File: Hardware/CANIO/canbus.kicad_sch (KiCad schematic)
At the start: 3 parts, among them J201 CAN, J202 CAN, U201 MCP25625-x-SS

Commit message: Add more boilerplate
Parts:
- added C201, C202: 22pf, Capacitor_SMD:C_0201_0603Metric, symbol Device:C_Small
- added C203, C204, C205: 100nf, Capacitor_SMD:C_0805_2012Metric, symbol Device:C_Small
- added R201: 120R, Resistor_THT:R_Axial_DIN0207_L6.3mm_D2.5mm_P10.16mm_Horizontal, symbol Device:R_Small
- added R202: 120R, Resistor_SMD:R_0805_2012Metric, symbol Device:R_Small
- added Y201: 16mHz, Crystal:Crystal_SMD_HC49-SD, symbol Device:Crystal
- J201, J202: footprint (none) -> Connector_Wire:SolderWire-0.5sqmm_1x02_P4.8mm_D0.9mm_OD2.3mm_Relief
- U201: LCSC# (none) -> C628816
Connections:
- net +5V: now also U201.1 (VIO), U201.19 (VDD), C203.1, C204.1, C205.1
- net CANH: now also R201.2
- net CANL: now also R201.1
- net GND: now reaches U201.10 (GND)
- net GND: now also U201.26 (VSS), C201.1, C202.2, C203.2, C204.2, C205.2, R202.1
- net SCK: now reaches U201.14 (SCK)
- net SI: now reaches U201.15 (SI)
- net SO: now reaches U201.16 (SO)
- net CS: now reaches U201.17 (~{CS})
- net CLKOUT: now reaches U201.22 (CLKOUT)
- net at U201.5 (STBY): now also R202.2
- net at U201.8 (OSC2): now also C202.1, Y201.1
- net at U201.9 (OSC1): now also C201.2, Y201.2
- no-connect marks 0 -> 7

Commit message: Add processor
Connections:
- net INT: now reaches U201.13 (~{INT})
- net STBY: now reaches R202.2, U201.5 (STBY)
- no-connect marks 7 -> 6
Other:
- note added: "INT lets us know if there is activity we need to see"
- note added: "Im not really planning on using standby mode, but the chip does offer some nice power saving and resume options! See page 7 in the datasheet for details"
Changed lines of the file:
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@@
   (junction (at 184.785 109.855) (diameter 0) (color 0 0 0 0)
+  )
+  (junction (at 108.585 78.105) (diameter 0) (color 0 0 0 0)
   )
   (junction (at 141.605 71.755) (diameter 0) (color 0 0 0 0)
@@
   (no_connect (at 131.445 113.665))
   (no_connect (at 131.445 100.965))
-  (no_connect (at 131.445 118.745))
   (no_connect (at 131.445 103.505))
+  (wire (pts (xy 125.73 118.745) (xy 131.445 118.745))
+    (stroke (width 0) (type default))
+  )
   (wire (pts (xy 141.605 71.755) (xy 141.605 73.025))
     (stroke (width 0) (type default))
@@
     (stroke (width 0) (type default))
   )
+  (wire (pts (xy 99.695 78.105) (xy 108.585 78.105))
+    (stroke (width 0) (type default))
+  )
   (wire (pts (xy 243.84 69.85) (xy 234.95 69.85))
     (stroke (width 0) (type default))
@@
     (stroke (width 0) (type default))
   )
+  (text "INT lets us know\nif there is activity\nwe need to see"
+    (at 100.965 120.65 0)
+    (effects (font (size 1.27 1.27)) (justify left bottom))
+  )
+  (text "Im not really planning\non using standby mode, but the\nchip does offer some nice\npower saving and resume options!\n\nSee page 7 in the datasheet for details"
+    (at 52.07 87.63 0)
+    (effects (font (size 1.27 1.27)) (justify left bottom))
+  )
   (label "CANL" (at 170.815 80.645 180) (fields_autoplaced)
     (effects (font (size 1.27 1.27)) (justify right bottom))
@@
     (effects (font (size 1.27 1.27)) (justify right))
   )
+  (hierarchical_label "INT" (shape output) (at 125.73 118.745 180) (fields_autoplaced)
+    (effects (font (size 1.27 1.27)) (justify right))
+  )
   (hierarchical_label "SO" (shape output) (at 125.73 88.265 180) (fields_autoplaced)
     (effects (font (size 1.27 1.27)) (justify right))
@@
     (effects (font (size 1.27 1.27)) (justify right))
   )
+  (hierarchical_label "STBY" (shape input) (at 99.695 78.105 180) (fields_autoplaced)
+    (effects (font (size 1.27 1.27)) (justify right))
+  )

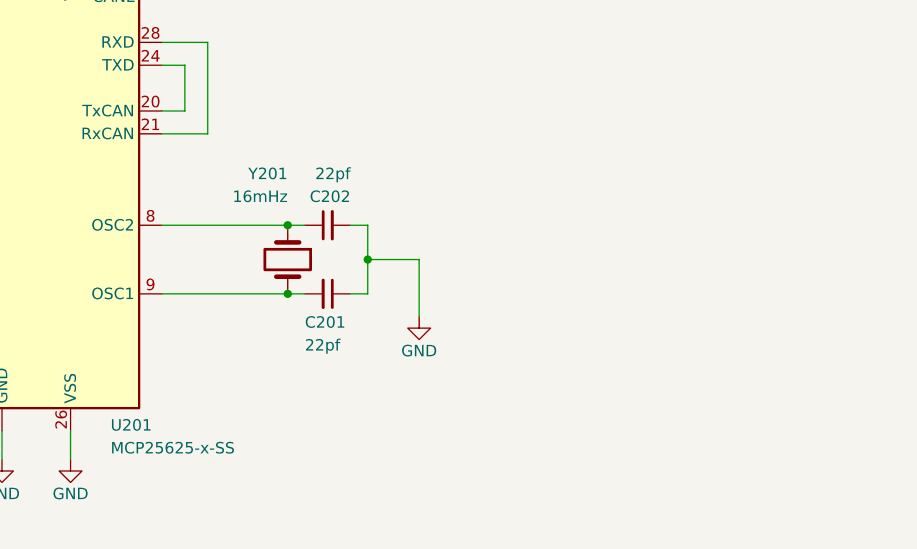
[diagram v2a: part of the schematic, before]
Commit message: Edge cuts and stuff
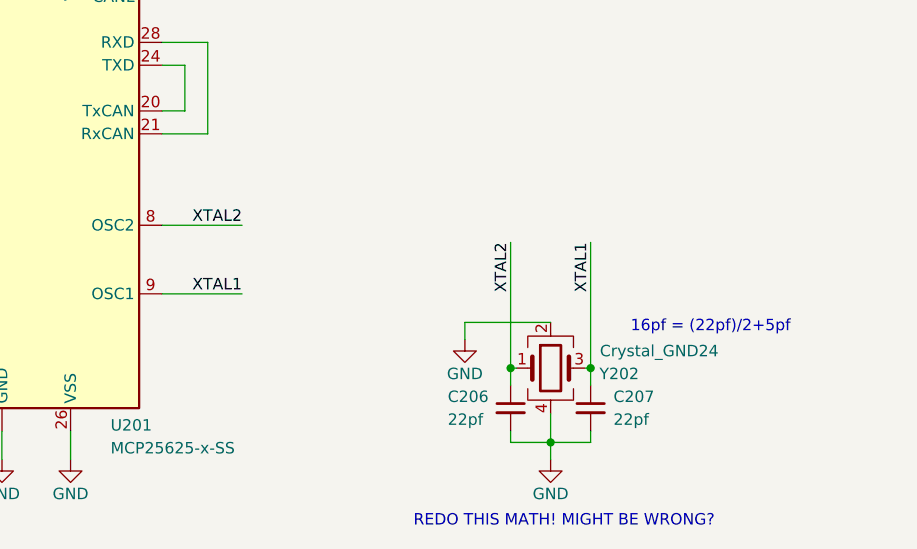
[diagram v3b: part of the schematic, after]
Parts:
- removed C201, C202: 22pf, Capacitor_SMD:C_0201_0603Metric, symbol Device:C_Small
- removed Y201: 16mHz, Crystal:Crystal_SMD_HC49-SD, symbol Device:Crystal
- added C206, C207: 22pf, Capacitor_SMD:C_0603_1608Metric, symbol Device:C_Small
- added Y202: Crystal_GND24, Crystal:Crystal_SMD_3225-4Pin_3.2x2.5mm, symbol Device:Crystal_GND24
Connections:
- net GND: now also C206.2, C207.2, Y202.2, Y202.4
- net XTAL2: now reaches U201.8 (OSC2)
- net XTAL2: now also C206.1, Y202.1
- net XTAL1: now reaches U201.9 (OSC1)
- net XTAL1: now also C207.1, Y202.3
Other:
- note added: "16pf = (22pf)/2+5pf"
- note added: "REDO THIS MATH! MIGHT BE WRONG?"

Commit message: Do some routing
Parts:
- added TP201, TP202, TP203: TestPoint, TestPoint:TestPoint_Pad_2.0x2.0mm, symbol Connector:TestPoint
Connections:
- net CLKOUT: now also TP203.1
- net at U201.20 (TxCAN), U201.24 (TXD): now also TP202.1
- net at U201.21 (RxCAN), U201.28 (RXD): now also TP201.1
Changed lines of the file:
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@@
   (junction (at 200.66 121.92) (diameter 0) (color 0 0 0 0)
+  )
+  (junction (at 167.005 85.725) (diameter 0) (color 0 0 0 0)
+  )
+  (junction (at 164.465 93.345) (diameter 0) (color 0 0 0 0)
+  )
+  (junction (at 127.635 123.825) (diameter 0) (color 0 0 0 0)
   )
   (junction (at 205.105 130.175) (diameter 0) (color 0 0 0 0)
@@
     (stroke (width 0) (type default))
   )
-  (wire (pts (xy 125.73 123.825) (xy 131.445 123.825))
+  (wire (pts (xy 125.73 123.825) (xy 127.635 123.825))
     (stroke (width 0) (type default))
   )
@@
     (stroke (width 0) (type default))
   )
+  (wire (pts (xy 168.91 85.725) (xy 167.005 85.725))
+    (stroke (width 0) (type default))
+  )
   (wire (pts (xy 170.815 80.645) (xy 161.925 80.645))
     (stroke (width 0) (type default))
@@
     (stroke (width 0) (type default))
   )
-  (wire (pts (xy 164.465 93.345) (xy 161.925 93.345))
+  (wire (pts (xy 161.925 93.345) (xy 164.465 93.345))
     (stroke (width 0) (type default))
   )
@@
     (stroke (width 0) (type default))
   )
+  (wire (pts (xy 164.465 93.345) (xy 168.91 93.345))
+    (stroke (width 0) (type default))
+  )
   (wire (pts (xy 132.715 62.23) (xy 132.715 63.5))
     (stroke (width 0) (type default))
@@
   )
   (wire (pts (xy 195.58 118.745) (xy 195.58 116.84))
+    (stroke (width 0) (type default))
+  )
+  (wire (pts (xy 127.635 123.825) (xy 131.445 123.825))
     (stroke (width 0) (type default))
   )
@@
     )
   )
+  (symbol (lib_id "Connector:TestPoint") (at 168.91 85.725 270) (unit 1)
+    (in_bom yes) (on_board yes) (dnp no)
+    (property "Reference" "TP201" (at 173.99 85.725 90)
+      (effects (font (size 1.27 1.27)) (justify left))
+    )
+    (property "Value" "TestPoint" (at 174.625 86.995 90)
+      (effects (font (size 1.27 1.27)) (justify left) hide)
+    )
+    (property "Footprint" "TestPoint:TestPoint_Pad_2.0x2.0mm" (at 168.91 90.805 0)
+      (effects (font (size 1.27 1.27)) hide)
+    )
+    (property "Datasheet" "~" (at 168.91 90.805 0)
+      (effects (font (size 1.27 1.27)) hide)
+    )
+    (pin "1")
+    (instances
+      (project "CANIO"
+        (path "/894f620e-3404-4a40-a2a7-513bc1d5f99b/de3f136a-4876-4908-a268-32055f46152a"
+          (reference "TP201") (unit 1)
+        )
+      )
+    )
+  )
   (symbol (lib_id "power:GND") (at 144.145 132.08 0) (unit 1)
     (in_bom yes) (on_board yes) (dnp no)
@@
       (effects (font (size 1.27 1.27)) hide)
     )
-    (property "Datasheet" "http://ww1.microchip.com/downloads/en/DeviceDoc/20005282B.pdf" (at 146.685 85.725 0)
+    (property "Datasheet" "https://datasheet.lcsc.com/lcsc/2012231242_Microchip-Tech-MCP25625T-E-SS_C628816.pdf" (at 146.685 85.725 0)
       (effects (font (size 1.27 1.27)) hide)
     )
@@
     )
   )
+  (symbol (lib_id "Connector:TestPoint") (at 127.635 123.825 180) (unit 1)
+    (in_bom yes) (on_board yes) (dnp no)
+    (property "Reference" "TP203" (at 127.635 128.905 90)
+      (effects (font (size 1.27 1.27)) (justify left))
+    )
+    (property "Value" "TestPoint" (at 126.365 129.54 90)
+      (effects (font (size 1.27 1.27)) (justify left) hide)
+    )
+    (property "Footprint" "TestPoint:TestPoint_Pad_2.0x2.0mm" (at 122.555 123.825 0)
+      (effects (font (size 1.27 1.27)) hide)
+    )
+    (property "Datasheet" "~" (at 122.555 123.825 0)
+      (effects (font (size 1.27 1.27)) hide)
+    )
+    (pin "1")
+    (instances
+      (project "CANIO"
+        (path "/894f620e-3404-4a40-a2a7-513bc1d5f99b/de3f136a-4876-4908-a268-32055f46152a"
+          (reference "TP203") (unit 1)
+        )
+      )
+    )
+  )
   (symbol (lib_id "Device:C_Small") (at 122.555 59.69 0) (unit 1)
     (in_bom yes) (on_board yes) (dnp no)
@@
         )
       )
+    )
+  )
+  (symbol (lib_id "Connector:TestPoint") (at 168.91 93.345 270) (unit 1)
+    (in_bom yes) (on_board yes) (dnp no)
+    (property "Reference" "TP202" (at 173.99 93.345 90)
+      (effects (font (size 1.27 1.27)) (justify left))
+    )
+    (property "Value" "TestPoint" (at 174.625 94.615 90)
+      (effects (font (size 1.27 1.27)) (justify left) hide)
+    )
+    (property "Footprint" "TestPoint:TestPoint_Pad_2.0x2.0mm" (at 168.91 98.425 0)
+      (effects (font (size 1.27 1.27)) hide)
+    )
+    (property "Datasheet" "~" (at 168.91 98.425 0)
+      (effects (font (size 1.27 1.27)) hide)
+    )
+    (pin "1")
+    (instances
+      (project "CANIO"
+        (path "/894f620e-3404-4a40-a2a7-513bc1d5f99b/de3f136a-4876-4908-a268-32055f46152a"
+          (reference "TP202") (unit 1)
+        )
+      )

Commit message: Everything seems ship shape
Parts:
- added D201: ACT, LED_SMD:LED_0805_2012Metric, symbol Device:LED
- added D202: DNP, LED_SMD:LED_0805_2012Metric, symbol Device:LED
- added R203: 1K, Resistor_SMD:R_0805_2012Metric, symbol Device:R_Small
- added R204: DNP, Resistor_SMD:R_0805_2012Metric, symbol Device:R_Small
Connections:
- net +5V: now also D201.2 (A), D202.2 (A)
- net at TP201.1, U201.21 (RxCAN), U201.28 (RXD): now also R203.1
- net at TP202.1, U201.20 (TxCAN), U201.24 (TXD): now also R204.1
- new net: D201.1 (K), R203.2
- new net: D202.1 (K), R204.2
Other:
- note added: "Datasheet says RXD goes LOW when can ACT/Change, also going LOW is how the controller knows when the bus is resuming."
- moved on the sheet: TP201, TP202
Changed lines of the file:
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@@
 (kicad_sch (version 20230121) (generator eeschema)
   (paper "A4")
+  (junction (at 175.26 85.725) (diameter 0) (color 0 0 0 0)
+  )
   (junction (at 108.585 78.105) (diameter 0) (color 0 0 0 0)
   )
@@
   )
   (junction (at 164.465 93.345) (diameter 0) (color 0 0 0 0)
+  )
+  (junction (at 175.26 93.345) (diameter 0) (color 0 0 0 0)
+  )
+  (junction (at 203.835 85.725) (diameter 0) (color 0 0 0 0)
   )
   (junction (at 127.635 123.825) (diameter 0) (color 0 0 0 0)
@@
     (stroke (width 0) (type default))
   )
+  (wire (pts (xy 203.835 85.725) (xy 199.39 85.725))
+    (stroke (width 0) (type default))
+  )
   (wire (pts (xy 125.73 90.805) (xy 131.445 90.805))
     (stroke (width 0) (type default))
@@
     (stroke (width 0) (type default))
   )
+  (wire (pts (xy 175.26 85.725) (xy 184.15 85.725))
+    (stroke (width 0) (type default))
+  )
   (wire (pts (xy 122.555 55.88) (xy 122.555 57.15))
     (stroke (width 0) (type default))
   )
-  (wire (pts (xy 168.91 85.725) (xy 167.005 85.725))
-    (stroke (width 0) (type default))
-  )
   (wire (pts (xy 170.815 80.645) (xy 161.925 80.645))
     (stroke (width 0) (type default))
@@
     (stroke (width 0) (type default))
   )
-  (wire (pts (xy 164.465 93.345) (xy 168.91 93.345))
+  (wire (pts (xy 164.465 93.345) (xy 175.26 93.345))
     (stroke (width 0) (type default))
   )
@@
     (stroke (width 0) (type default))
   )
+  (wire (pts (xy 203.835 93.345) (xy 199.39 93.345))
+    (stroke (width 0) (type default))
+  )
   (wire (pts (xy 161.925 95.885) (xy 167.005 95.885))
     (stroke (width 0) (type default))
   )
+  (wire (pts (xy 189.23 85.725) (xy 191.77 85.725))
+    (stroke (width 0) (type default))
+  )
   (wire (pts (xy 161.925 113.665) (xy 170.815 113.665))
     (stroke (width 0) (type default))
@@
     (stroke (width 0) (type default))
   )
+  (wire (pts (xy 189.23 93.345) (xy 191.77 93.345))
+    (stroke (width 0) (type default))
+  )
   (wire (pts (xy 161.925 88.265) (xy 164.465 88.265))
     (stroke (width 0) (type default))
@@
     (stroke (width 0) (type default))
   )
+  (wire (pts (xy 203.835 93.345) (xy 203.835 85.725))
+    (stroke (width 0) (type default))
+  )
   (wire (pts (xy 127.635 123.825) (xy 131.445 123.825))
     (stroke (width 0) (type default))
@@
     (stroke (width 0) (type default))
   )
+  (wire (pts (xy 175.26 93.345) (xy 184.15 93.345))
+    (stroke (width 0) (type default))
+  )
   (wire (pts (xy 108.585 78.105) (xy 108.585 79.375))
     (stroke (width 0) (type default))
@@
   )
   (wire (pts (xy 209.55 121.92) (xy 209.55 123.825))
+    (stroke (width 0) (type default))
+  )
+  (wire (pts (xy 167.005 85.725) (xy 175.26 85.725))
+    (stroke (width 0) (type default))
+  )
+  (wire (pts (xy 203.835 83.185) (xy 203.835 85.725))
     (stroke (width 0) (type default))
   )
@@
     (effects (font (size 1.27 1.27)) (justify left bottom))
   )
+  (text "Datasheet says RXD goes LOW\nwhen can ACT/Change, also going LOW\nis how the controller knows when the bus\nis resuming."
+    (at 205.74 92.71 0)
+    (effects (font (size 1.27 1.27)) (justify left bottom))
+  )
   (text "16pf = (22pf)/2+5pf" (at 231.775 118.11 0)
     (effects (font (size 1.27 1.27)) (justify right bottom))
@@
     )
   )
+  (symbol (lib_id "Device:R_Small") (at 186.69 85.725 90) (unit 1)
+    (in_bom yes) (on_board yes) (dnp no)
+    (property "Reference" "R203" (at 186.69 80.645 90)
+      (effects (font (size 1.27 1.27)))
+    )
+    (property "Value" "1K" (at 186.69 83.185 90)
+      (effects (font (size 1.27 1.27)))
+    )
+    (property "Footprint" "Resistor_SMD:R_0805_2012Metric" (at 186.69 85.725 0)
+      (effects (font (size 1.27 1.27)) hide)
+    )
+    (property "Datasheet" "~" (at 186.69 85.725 0)
+      (effects (font (size 1.27 1.27)) hide)
+    )
+    (pin "1")
+    (pin "2")
+    (instances
+      (project "CANIO"
+        (path "/894f620e-3404-4a40-a2a7-513bc1d5f99b/de3f136a-4876-4908-a268-32055f46152a"
+          (reference "R203") (unit 1)
+        )
+      )
+    )
+  )
   (symbol (lib_id "power:+5V") (at 151.765 70.485 0) (unit 1)
     (in_bom yes) (on_board yes) (dnp no)
@@
     )
   )
-  (symbol (lib_id "Connector:TestPoint") (at 168.91 85.725 270) (unit 1)
-    (in_bom yes) (on_board yes) (dnp no)
-    (property "Reference" "TP201" (at 173.99 85.725 90)
-      (effects (font (size 1.27 1.27)) (justify left))
-    )
-    (property "Value" "TestPoint" (at 174.625 86.995 90)
+  (symbol (lib_id "Connector:TestPoint") (at 175.26 85.725 0) (unit 1)
+    (in_bom yes) (on_board yes) (dnp no)
+    (property "Reference" "TP201" (at 172.72 80.645 0)
+      (effects (font (size 1.27 1.27)) (justify left))
+    )
+    (property "Value" "TestPoint" (at 176.53 80.01 90)
       (effects (font (size 1.27 1.27)) (justify left) hide)
     )
-    (property "Footprint" "TestPoint:TestPoint_Pad_2.0x2.0mm" (at 168.91 90.805 0)
-      (effects (font (size 1.27 1.27)) hide)
-    )
-    (property "Datasheet" "~" (at 168.91 90.805 0)
+    (property "Footprint" "TestPoint:TestPoint_Pad_2.0x2.0mm" (at 180.34 85.725 0)
+      (effects (font (size 1.27 1.27)) hide)
+    )
+    (property "Datasheet" "~" (at 180.34 85.725 0)
       (effects (font (size 1.27 1.27)) hide)
     )
@@
         (path "/894f620e-3404-4a40-a2a7-513bc1d5f99b/de3f136a-4876-4908-a268-32055f46152a"
           (reference "#PWR0205") (unit 1)
+        )
+      )
+    )
+  )
+  (symbol (lib_id "power:+5V") (at 203.835 83.185 0) (unit 1)
+    (in_bom yes) (on_board yes) (dnp no)
+    (property "Reference" "#PWR0202" (at 203.835 86.995 0)
+      (effects (font (size 1.27 1.27)) hide)
+    )
+    (property "Value" "+5V" (at 203.835 79.375 0)
+      (effects (font (size 1.27 1.27)))
+    )
+    (property "Footprint" "" (at 203.835 83.185 0)
+      (effects (font (size 1.27 1.27)) hide)
+    )
+    (property "Datasheet" "" (at 203.835 83.185 0)
+      (effects (font (size 1.27 1.27)) hide)
+    )
+    (pin "1")
+    (instances
+      (project "CANIO"
+        (path "/894f620e-3404-4a40-a2a7-513bc1d5f99b/de3f136a-4876-4908-a268-32055f46152a"
+          (reference "#PWR0202") (unit 1)
         )
       )
@@
     )
   )
+  (symbol (lib_id "Device:LED") (at 195.58 93.345 0) (unit 1)
+    (in_bom yes) (on_board yes) (dnp no)
+    (property "Reference" "D202" (at 195.58 88.265 0)
+      (effects (font (size 1.27 1.27)))
+    )
+    (property "Value" "DNP" (at 195.58 90.805 0)
+      (effects (font (size 1.27 1.27)))
+    )
+    (property "Footprint" "LED_SMD:LED_0805_2012Metric" (at 195.58 93.345 0)
+      (effects (font (size 1.27 1.27)) hide)
+    )
+    (property "Datasheet" "~" (at 195.58 93.345 0)
+      (effects (font (size 1.27 1.27)) hide)
+    )
+    (pin "1")
+    (pin "2")
+    (instances
+      (project "CANIO"
+        (path "/894f620e-3404-4a40-a2a7-513bc1d5f99b/de3f136a-4876-4908-a268-32055f46152a"
+          (reference "D202") (unit 1)
+        )
+      )
+    )
+  )
   (symbol (lib_id "Connector:Conn_01x02_Socket") (at 213.36 61.595 0) (unit 1)
     (in_bom yes) (on_board yes) (dnp no) (fields_autoplaced)
@@
     )
   )
-  (symbol (lib_id "Connector:TestPoint") (at 168.91 93.345 270) (unit 1)
-    (in_bom yes) (on_board yes) (dnp no)
-    (property "Reference" "TP202" (at 173.99 93.345 90)
-      (effects (font (size 1.27 1.27)) (justify left))
-    )
-    (property "Value" "TestPoint" (at 174.625 94.615 90)
+  (symbol (lib_id "Connector:TestPoint") (at 175.26 93.345 180) (unit 1)
+    (in_bom yes) (on_board yes) (dnp no)
+    (property "Reference" "TP202" (at 177.8 99.06 0)
+      (effects (font (size 1.27 1.27)) (justify left))
+    )
+    (property "Value" "TestPoint" (at 173.99 99.06 90)
       (effects (font (size 1.27 1.27)) (justify left) hide)
     )
-    (property "Footprint" "TestPoint:TestPoint_Pad_2.0x2.0mm" (at 168.91 98.425 0)
-      (effects (font (size 1.27 1.27)) hide)
-    )
-    (property "Datasheet" "~" (at 168.91 98.425 0)
+    (property "Footprint" "TestPoint:TestPoint_Pad_2.0x2.0mm" (at 170.18 93.345 0)
+      (effects (font (size 1.27 1.27)) hide)
+    )
+    (property "Datasheet" "~" (at 170.18 93.345 0)
       (effects (font (size 1.27 1.27)) hide)
     )
@@
         (path "/894f620e-3404-4a40-a2a7-513bc1d5f99b/de3f136a-4876-4908-a268-32055f46152a"
           (reference "TP202") (unit 1)
+        )
+      )
+    )
+  )
+  (symbol (lib_id "Device:LED") (at 195.58 85.725 0) (unit 1)
+    (in_bom yes) (on_board yes) (dnp no)
+    (property "Reference" "D201" (at 195.58 80.645 0)
+      (effects (font (size 1.27 1.27)))
+    )
+    (property "Value" "ACT" (at 195.58 83.185 0)
+      (effects (font (size 1.27 1.27)))
+    )
+    (property "Footprint" "LED_SMD:LED_0805_2012Metric" (at 195.58 85.725 0)
+      (effects (font (size 1.27 1.27)) hide)
+    )
+    (property "Datasheet" "~" (at 195.58 85.725 0)
+      (effects (font (size 1.27 1.27)) hide)
+    )
+    (pin "1")
+    (pin "2")
+    (instances
+      (project "CANIO"
+        (path "/894f620e-3404-4a40-a2a7-513bc1d5f99b/de3f136a-4876-4908-a268-32055f46152a"
+          (reference "D201") (unit 1)
         )
       )
@@
         )
       )
+    )
+  )
+  (symbol (lib_id "Device:R_Small") (at 186.69 93.345 90) (unit 1)
+    (in_bom yes) (on_board yes) (dnp no)
+    (property "Reference" "R204" (at 186.69 88.265 90)
+      (effects (font (size 1.27 1.27)))
+    )
+    (property "Value" "DNP" (at 186.69 90.805 90)
+      (effects (font (size 1.27 1.27)))
+    )
+    (property "Footprint" "Resistor_SMD:R_0805_2012Metric" (at 186.69 93.345 0)
+      (effects (font (size 1.27 1.27)) hide)
+    )
+    (property "Datasheet" "~" (at 186.69 93.345 0)
+      (effects (font (size 1.27 1.27)) hide)
+    )
+    (pin "1")
+    (pin "2")
+    (instances
+      (project "CANIO"
+        (path "/894f620e-3404-4a40-a2a7-513bc1d5f99b/de3f136a-4876-4908-a268-32055f46152a"
+          (reference "R204") (unit 1)
+        )
+      )
